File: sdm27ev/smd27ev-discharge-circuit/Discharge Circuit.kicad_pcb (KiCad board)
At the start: 2 copper layers, 61.3 x 39.3 mm, 7 parts, among them J1 MPT-02-01-XX-X-RA-SD, J2 IPBT-102-H1-T-S-RA-K, J3 PET-02-01-T-VT-LC, K2 FTR-E1AA012Y-GR

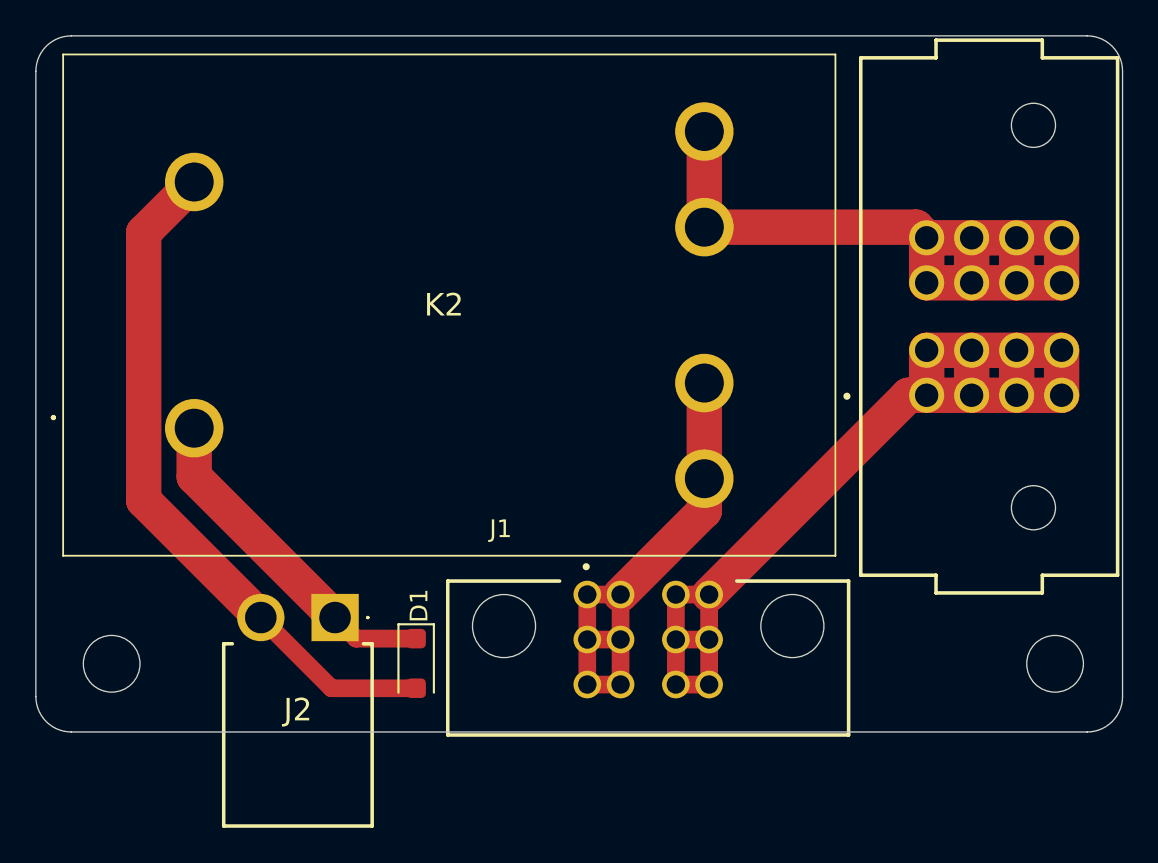
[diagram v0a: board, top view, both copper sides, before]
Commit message: Fixed discharge relay symbol/footprint
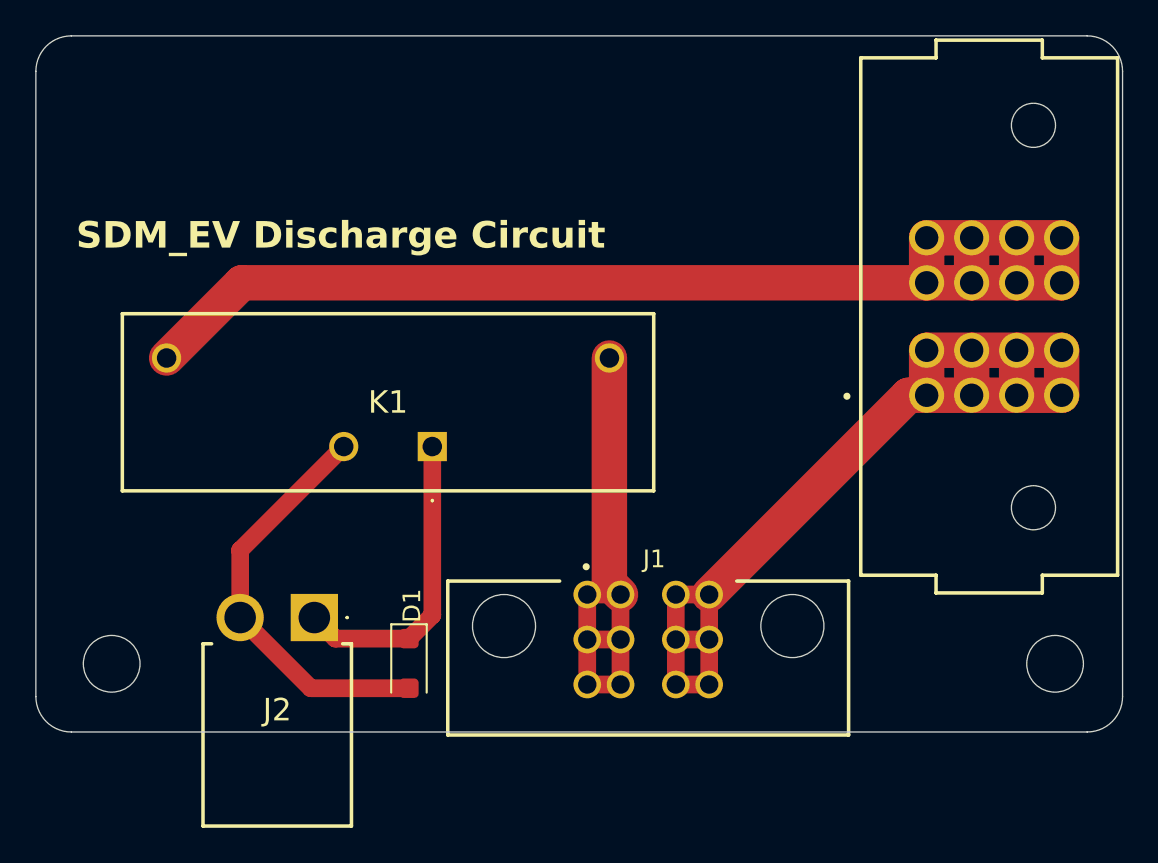
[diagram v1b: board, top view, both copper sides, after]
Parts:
- removed K2: FTR-E1AA012Y-GR, FTR-E1AA012Y-GR:FTRE1AA012YGR
- added K1: ~, footprint:S82405VHR, F.Cu at (122.2, 111.5)
- moved J2 1.17 mm to (115.6, 121.2)
- moved D1 0.41 mm to (120.9, 123.8)
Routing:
- net Net-(J3-Pad2): track 43.6 -> 70.1 mm
- net GND: track 38.9 -> 23.3 mm
- net Net-(D1-K): track 19.1 -> 17.2 mm
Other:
- board text added: "SDM_EV Discharge Circuit"
